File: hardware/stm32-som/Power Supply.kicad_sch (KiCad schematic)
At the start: 22 parts, among them Q1 DMP6023LE, U1 MCP16301, U2 AMS1117-3.3, U3 AMS1117-5.0

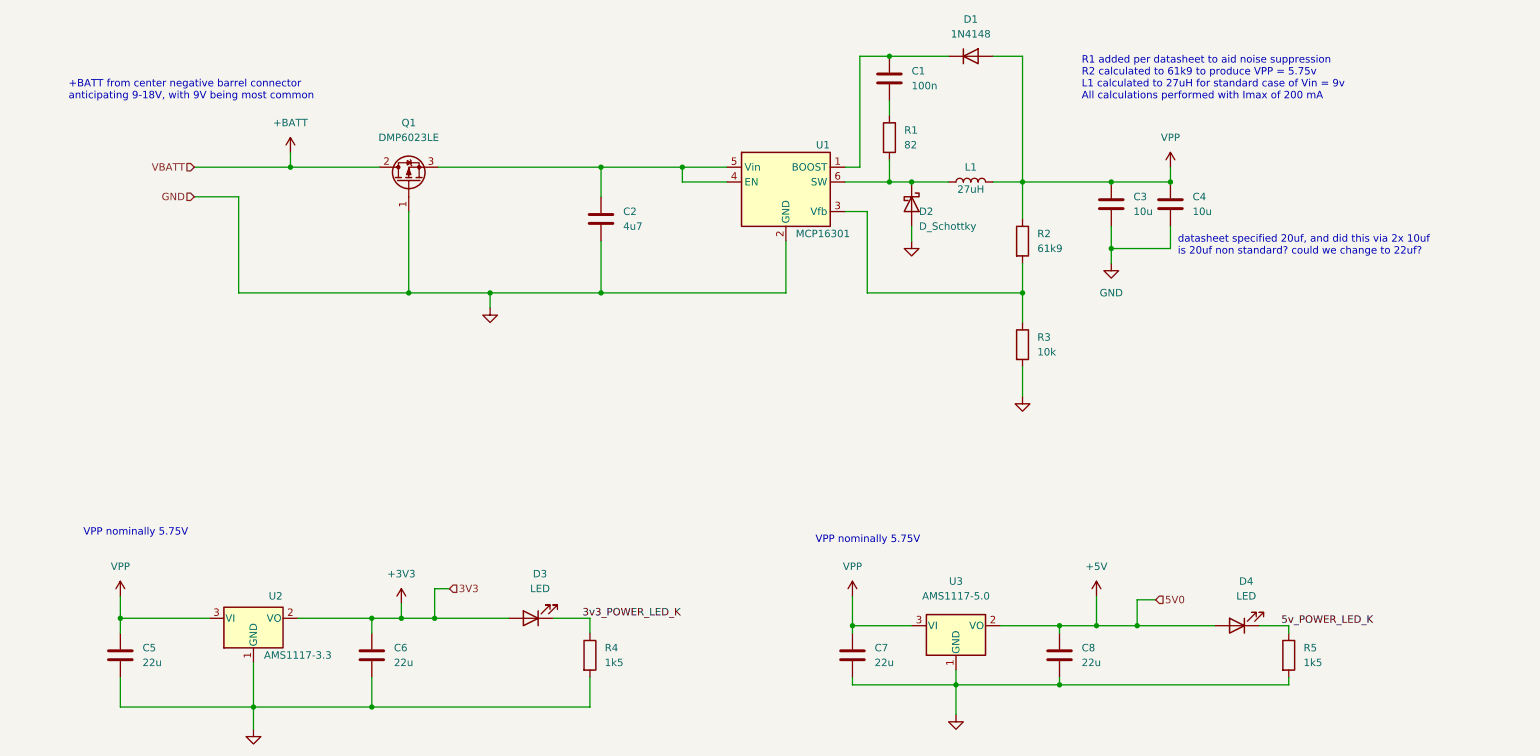
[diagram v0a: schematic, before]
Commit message: add test points, complete top hierarchical level, correct jtag mcu connection
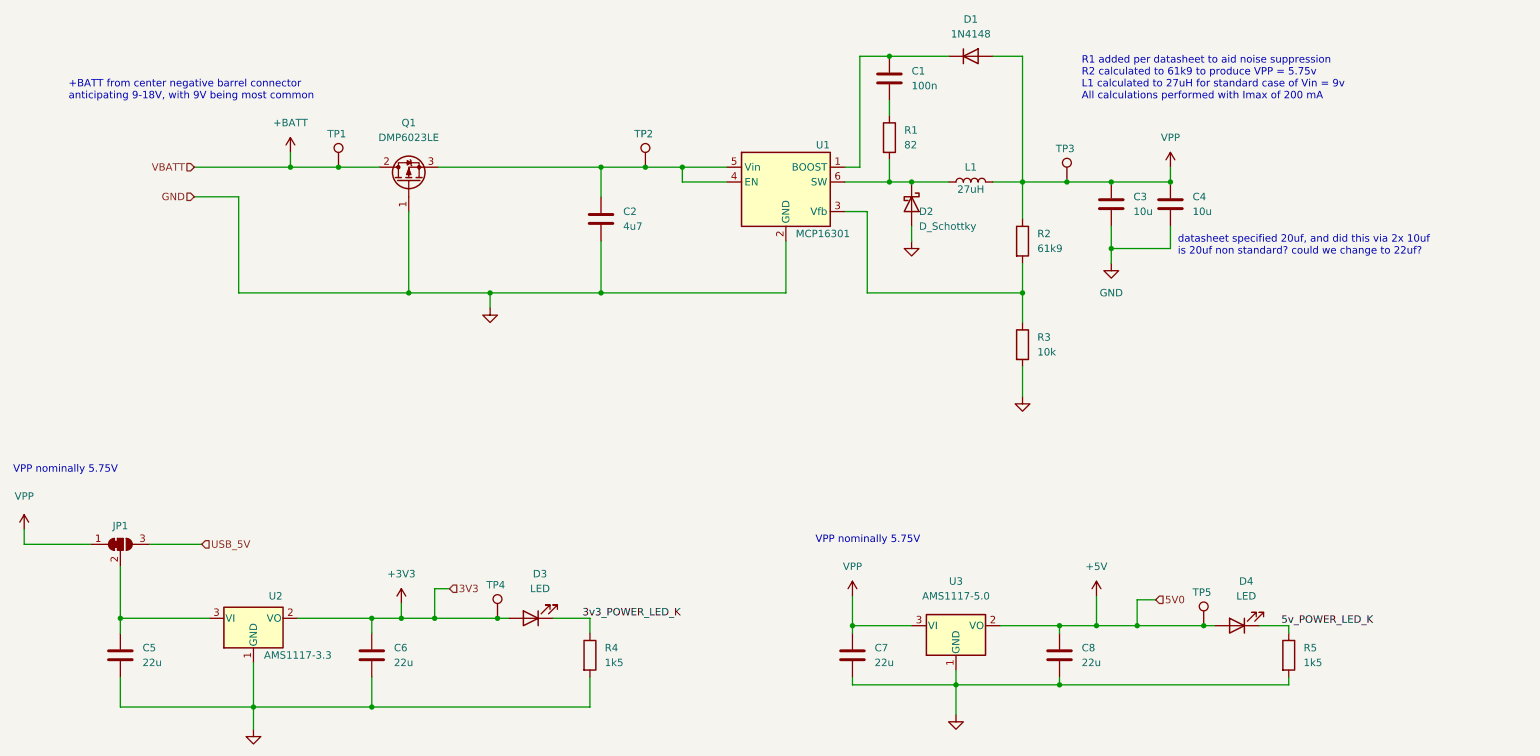
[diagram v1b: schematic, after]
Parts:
- added JP1: SolderJumper_3_Bridged12, symbol Jumper:SolderJumper_3_Bridged12
- added TP1, TP2, TP3, TP4, TP5: TestPoint, symbol Connector:TestPoint
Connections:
- net +3V3: now also TP4.1
- net +5V: now also TP5.1
- net +BATT: now also TP1.1
- net VPP: now also JP1.1 (A), TP3.1; no longer C5.1, U2.3 (VI)
- net at C2.1, Q1.3 (S), U1.4 (EN)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: now also TP2.1
- new net: C5.1, JP1.2 (C), U2.3 (VI)
- new net USB_5V: JP1.3 (B)

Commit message: clear ERC, small question about voltage level and rail timing on VCAP, but otherwise net name stuff
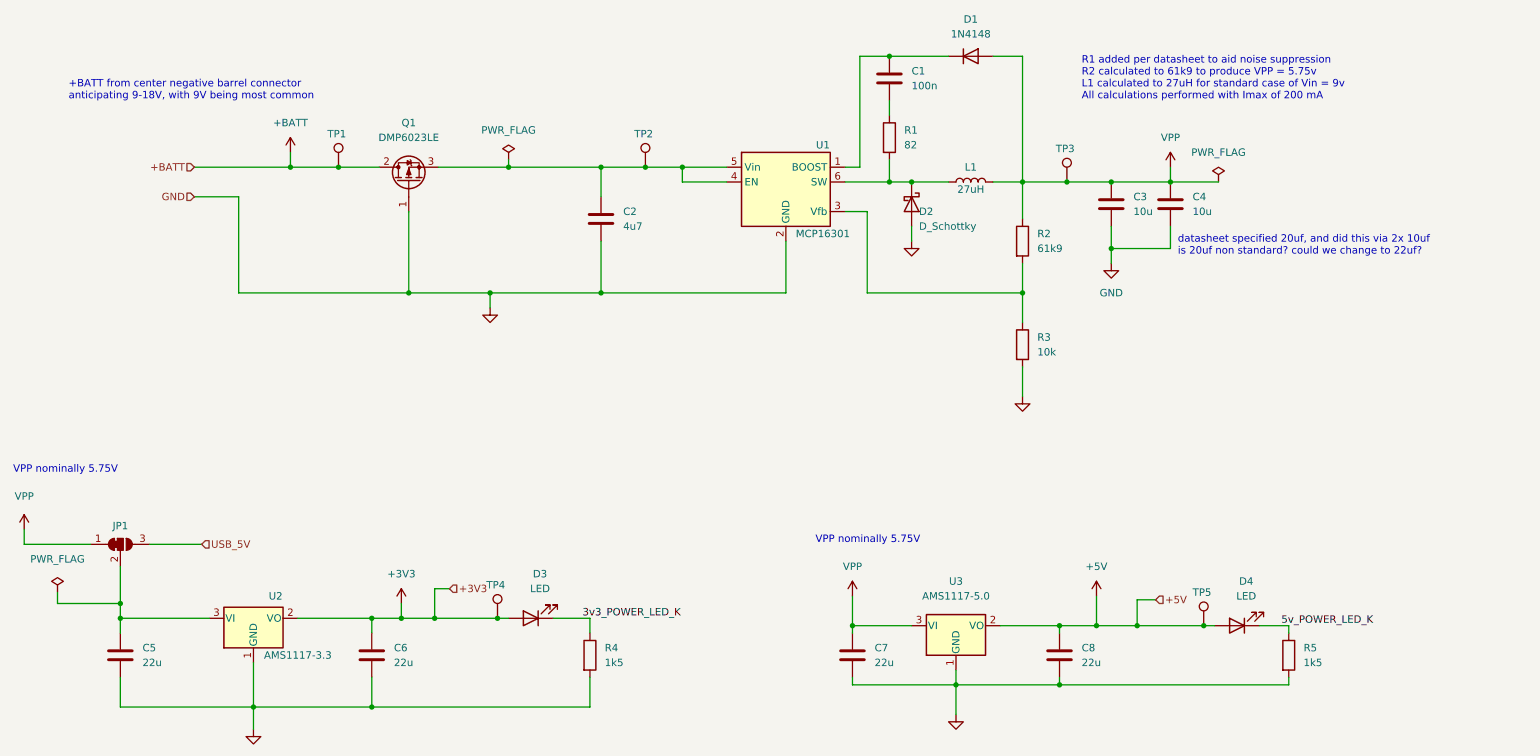
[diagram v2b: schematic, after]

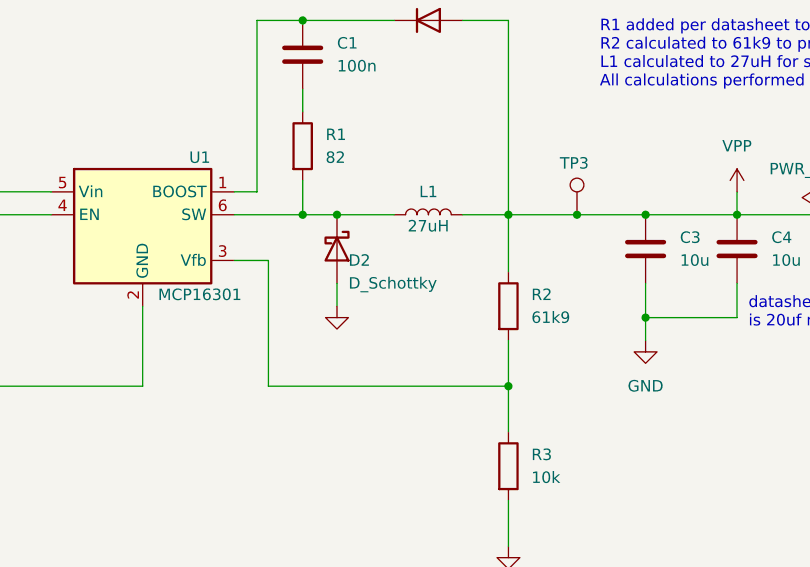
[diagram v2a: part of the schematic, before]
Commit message: add footprints to all components, JLC part numbers to to everything except capacitors and resistors
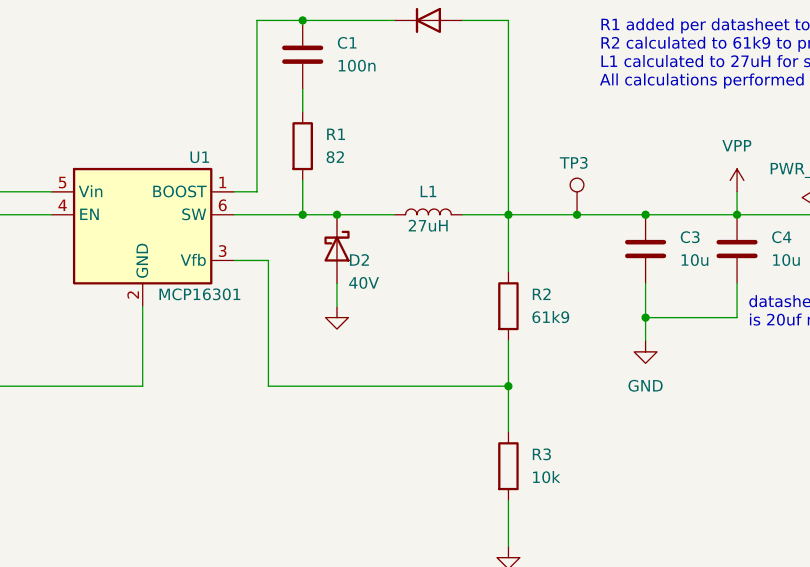
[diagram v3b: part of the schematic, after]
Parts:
- C1: footprint (none) -> Capacitor_SMD:C_0402_1005Metric
- C2, C3, C4, C5, C6, C7, C8: footprint (none) -> Capacitor_SMD:C_0805_2012Metric
- D1: footprint (none) -> Diode_SMD:D_SOD-123; JLC (none) -> C727110
- D2: value D_Schottky -> 40V; footprint (none) -> Diode_SMD:D_SOD-123; JLC (none) -> C8598
- D3, D4: footprint (none) -> LED_SMD:LED_0603_1608Metric; JLC (none) -> C2286
- JP1: footprint (none) -> Jumper:SolderJumper-3_P1.3mm_Bridged12_Pad1.0x1.5mm_NumberLabels
- L1: footprint (none) -> Inductor_SMD:L_1812_4532Metric; JLC (none) -> C394126; JLC-ALT (none) -> C394094
- Q1: footprint (none) -> Package_TO_SOT_SMD:SOT-223-3_TabPin2; JLC (none) -> C154901
- R1: footprint (none) -> Resistor_SMD:R_0603_1608Metric
- R2, R3: footprint (none) -> Resistor_SMD:R_0805_2012Metric
- R4, R5: footprint (none) -> Resistor_SMD:R_0402_1005Metric
- TP1, TP2, TP3, TP4, TP5: footprint (none) -> TestPoint:TestPoint_Loop_D2.54mm_Drill1.5mm_Beaded
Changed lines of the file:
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@@
       (effects (font (size 1.27 1.27)) (justify left))
     )
-    (property "Footprint" "" (id 2) (at 111.887 134.62 90)
+    (property "Footprint" "Resistor_SMD:R_0402_1005Metric" (id 2) (at 111.887 134.62 90)
       (effects (font (size 1.27 1.27)) hide)
     )
@@
       (effects (font (size 1.27 1.27)) (justify left))
     )
-    (property "Footprint" "" (id 2) (at 166.0652 39.37 0)
+    (property "Footprint" "Capacitor_SMD:C_0402_1005Metric" (id 2) (at 166.0652 39.37 0)
       (effects (font (size 1.27 1.27)) hide)
     )
@@
       (effects (font (size 1.27 1.27)) (justify left))
     )
-    (property "Footprint" "" (id 2) (at 186.182 63.5 90)
+    (property "Footprint" "Resistor_SMD:R_0805_2012Metric" (id 2) (at 186.182 63.5 90)
       (effects (font (size 1.27 1.27)) hide)
     )
@@
     (property "Reference" "D1" (id 0) (at 179.07 25.4 0))
     (property "Value" "1N4148" (id 1) (at 179.07 27.94 0))
-    (property "Footprint" "" (id 2) (at 179.07 31.75 0)
+    (property "Footprint" "Diode_SMD:D_SOD-123" (id 2) (at 179.07 31.75 0)
       (effects (font (size 1.27 1.27)) hide)
     )
     (property "Datasheet" "~" (id 3) (at 179.07 31.75 0)
+      (effects (font (size 1.27 1.27)) hide)
+    )
+    (property "JLC" "C727110" (id 4) (at 179.07 31.75 0)
       (effects (font (size 1.27 1.27)) hide)
     )
@@
       (effects (font (size 1.27 1.27)) (justify left))
     )
-    (property "Footprint" "" (id 2) (at 163.322 45.72 90)
+    (property "Footprint" "Resistor_SMD:R_0603_1608Metric" (id 2) (at 163.322 45.72 90)
       (effects (font (size 1.27 1.27)) hide)
     )
@@
       (effects (font (size 1.27 1.27)) (justify left))
     )
-    (property "Footprint" "" (id 2) (at 204.1652 60.96 0)
+    (property "Footprint" "Capacitor_SMD:C_0805_2012Metric" (id 2) (at 204.1652 60.96 0)
       (effects (font (size 1.27 1.27)) hide)
     )
@@
     (property "Reference" "Q1" (id 0) (at 82.55 43.18 90))
     (property "Value" "DMP6023LE" (id 1) (at 82.55 45.72 90))
-    (property "Footprint" "" (id 2) (at 80.01 48.26 0)
+    (property "Footprint" "Package_TO_SOT_SMD:SOT-223-3_TabPin2" (id 2) (at 80.01 48.26 0)
       (effects (font (size 1.27 1.27)) hide)
     )
     (property "Datasheet" "~" (id 3) (at 82.55 53.34 0)
+      (effects (font (size 1.27 1.27)) hide)
+    )
+    (property "JLC" "C154901" (id 4) (at 82.55 53.34 90)
       (effects (font (size 1.27 1.27)) hide)
     )
@@
       (effects (font (size 1.27 1.27)) hide)
     )
-    (property "Footprint" "" (id 2) (at 33.02 115.57 0)
+    (property "Footprint" "Jumper:SolderJumper-3_P1.3mm_Bridged12_Pad1.0x1.5mm_NumberLabels" (id 2) (at 33.02 115.57 0)
       (effects (font (size 1.27 1.27)) hide)
     )
@@
     (property "Reference" "D4" (id 0) (at 226.3775 121.92 0))
     (property "Value" "LED" (id 1) (at 226.3775 124.46 0))
-    (property "Footprint" "" (id 2) (at 224.79 129.54 0)
+    (property "Footprint" "LED_SMD:LED_0603_1608Metric" (id 2) (at 224.79 129.54 0)
       (effects (font (size 1.27 1.27)) hide)
     )
     (property "Datasheet" "~" (id 3) (at 224.79 129.54 0)
+      (effects (font (size 1.27 1.27)) hide)
+    )
+    (property "JLC" "C2286" (id 4) (at 224.79 129.54 0)
       (effects (font (size 1.27 1.27)) hide)
     )
@@
       (effects (font (size 1.27 1.27)) (justify left))
     )
-    (property "Footprint" "" (id 2) (at 33.9852 138.43 0)
+    (property "Footprint" "Capacitor_SMD:C_0805_2012Metric" (id 2) (at 33.9852 138.43 0)
       (effects (font (size 1.27 1.27)) hide)
     )
@@
       (effects (font (size 1.27 1.27)) (justify left))
     )
-    (property "Footprint" "" (id 2) (at 231.902 134.62 90)
+    (property "Footprint" "Resistor_SMD:R_0402_1005Metric" (id 2) (at 231.902 134.62 90)
       (effects (font (size 1.27 1.27)) hide)
     )
@@
     (property "Reference" "D3" (id 0) (at 105.0925 120.65 0))
     (property "Value" "LED" (id 1) (at 105.0925 123.19 0))
-    (property "Footprint" "" (id 2) (at 103.505 128.27 0)
+    (property "Footprint" "LED_SMD:LED_0603_1608Metric" (id 2) (at 103.505 128.27 0)
       (effects (font (size 1.27 1.27)) hide)
     )
@@
       (effects (font (size 1.27 1.27)) hide)
     )
+    (property "JLC" "C2286" (id 4) (at 103.505 128.27 0)
+      (effects (font (size 1.27 1.27)) hide)
+    )
     (pin "1")
     (pin "2")
@@
       (effects (font (size 1.27 1.27)) (justify left))
     )
-    (property "Footprint" "" (id 2) (at 195.2752 138.43 0)
+    (property "Footprint" "Capacitor_SMD:C_0805_2012Metric" (id 2) (at 195.2752 138.43 0)
       (effects (font (size 1.27 1.27)) hide)
     )
@@
       (effects (font (size 1.27 1.27)) (justify left) hide)
     )
-    (property "Footprint" "" (id 2) (at 102.87 128.27 0)
+    (property "Footprint" "TestPoint:TestPoint_Loop_D2.54mm_Drill1.5mm_Beaded" (id 2) (at 102.87 128.27 0)
       (effects (font (size 1.27 1.27)) hide)
     )
@@
       (effects (font (size 1.27 1.27)) (justify left))
     )
-    (property "Value" "D_Schottky" (id 1) (at 170.18 60.96 90)
-      (effects (font (size 1.27 1.27)) (justify left))
-    )
-    (property "Footprint" "" (id 2) (at 168.91 57.15 0)
+    (property "Value" "40V" (id 1) (at 170.18 60.96 90)
+      (effects (font (size 1.27 1.27)) (justify left))
+    )
+    (property "Footprint" "Diode_SMD:D_SOD-123" (id 2) (at 168.91 57.15 0)
       (effects (font (size 1.27 1.27)) hide)
     )
     (property "Datasheet" "~" (id 3) (at 168.91 57.15 0)
+      (effects (font (size 1.27 1.27)) hide)
+    )
+    (property "JLC" "C8598" (id 4) (at 168.91 57.15 90)
       (effects (font (size 1.27 1.27)) hide)
     )
@@
       (effects (font (size 1.27 1.27)) (justify left))
     )
-    (property "Footprint" "" (id 2) (at 186.182 81.28 90)
+    (property "Footprint" "Resistor_SMD:R_0805_2012Metric" (id 2) (at 186.182 81.28 90)
       (effects (font (size 1.27 1.27)) hide)
     )
@@
       (effects (font (size 1.27 1.27)) (justify left) hide)
     )
-    (property "Footprint" "" (id 2) (at 128.27 50.8 0)
+    (property "Footprint" "TestPoint:TestPoint_Loop_D2.54mm_Drill1.5mm_Beaded" (id 2) (at 128.27 50.8 0)
       (effects (font (size 1.27 1.27)) hide)
     )
@@
       (effects (font (size 1.27 1.27)) (justify left))
     )
-    (property "Footprint" "" (id 2) (at 116.5352 63.5 0)
+    (property "Footprint" "Capacitor_SMD:C_0805_2012Metric" (id 2) (at 116.5352 63.5 0)
       (effects (font (size 1.27 1.27)) hide)
     )
@@
       (effects (font (size 1.27 1.27)) (justify left))
     )
-    (property "Footprint" "" (id 2) (at 214.3252 60.96 0)
+    (property "Footprint" "Capacitor_SMD:C_0805_2012Metric" (id 2) (at 214.3252 60.96 0)
       (effects (font (size 1.27 1.27)) hide)
     )
@@
     (property "Reference" "L1" (id 0) (at 179.07 50.8 90))
     (property "Value" "27uH" (id 1) (at 179.07 54.61 90))
-    (property "Footprint" "" (id 2) (at 179.07 53.34 0)
+    (property "Footprint" "Inductor_SMD:L_1812_4532Metric" (id 2) (at 179.07 53.34 0)
       (effects (font (size 1.27 1.27)) hide)
     )
@@
       (effects (font (size 1.27 1.27)) hide)
     )
+    (property "JLC" "C394126" (id 4) (at 179.07 53.34 90)
+      (effects (font (size 1.27 1.27)) hide)
+    )
+    (property "JLC-ALT" "C394094" (id 5) (at 179.07 53.34 90)
+      (effects (font (size 1.27 1.27)) hide)
+    )
     (pin "1")
     (pin "2")
@@
       (effects (font (size 1.27 1.27)) (justify left))
     )
-    (property "Footprint" "" (id 2) (at 77.1652 138.43 0)
+    (property "Footprint" "Capacitor_SMD:C_0805_2012Metric" (id 2) (at 77.1652 138.43 0)
       (effects (font (size 1.27 1.27)) hide)
     )
@@
       (effects (font (size 1.27 1.27)) (justify left) hide)
     )
-    (property "Footprint" "" (id 2) (at 75.565 50.8 0)
+    (property "Footprint" "TestPoint:TestPoint_Loop_D2.54mm_Drill1.5mm_Beaded" (id 2) (at 75.565 50.8 0)
       (effects (font (size 1.27 1.27)) hide)
     )
@@
       (effects (font (size 1.27 1.27)) (justify left) hide)
     )
-    (property "Footprint" "" (id 2) (at 224.155 129.54 0)
+    (property "Footprint" "TestPoint:TestPoint_Loop_D2.54mm_Drill1.5mm_Beaded" (id 2) (at 224.155 129.54 0)
       (effects (font (size 1.27 1.27)) hide)
     )
@@
       (effects (font (size 1.27 1.27)) (justify left))
     )
-    (property "Footprint" "" (id 2) (at 159.7152 138.43 0)
+    (property "Footprint" "Capacitor_SMD:C_0805_2012Metric" (id 2) (at 159.7152 138.43 0)
       (effects (font (size 1.27 1.27)) hide)
     )
@@
       (effects (font (size 1.27 1.27)) (justify left) hide)
     )
-    (property "Footprint" "" (id 2) (at 200.66 53.34 0)
-      (effects (font (size 1.27 1.27)) hide)
-    )
+    (property "Footprint" "TestPoint:TestPoint_Loop_D2.54mm_Drill1.5mm_Beaded" (id 2) (at 200.66 53.34 0)
+      (effects (font (size 1.27 1.27)) hide)
+    )
